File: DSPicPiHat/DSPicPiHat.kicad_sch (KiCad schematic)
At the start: 84 parts

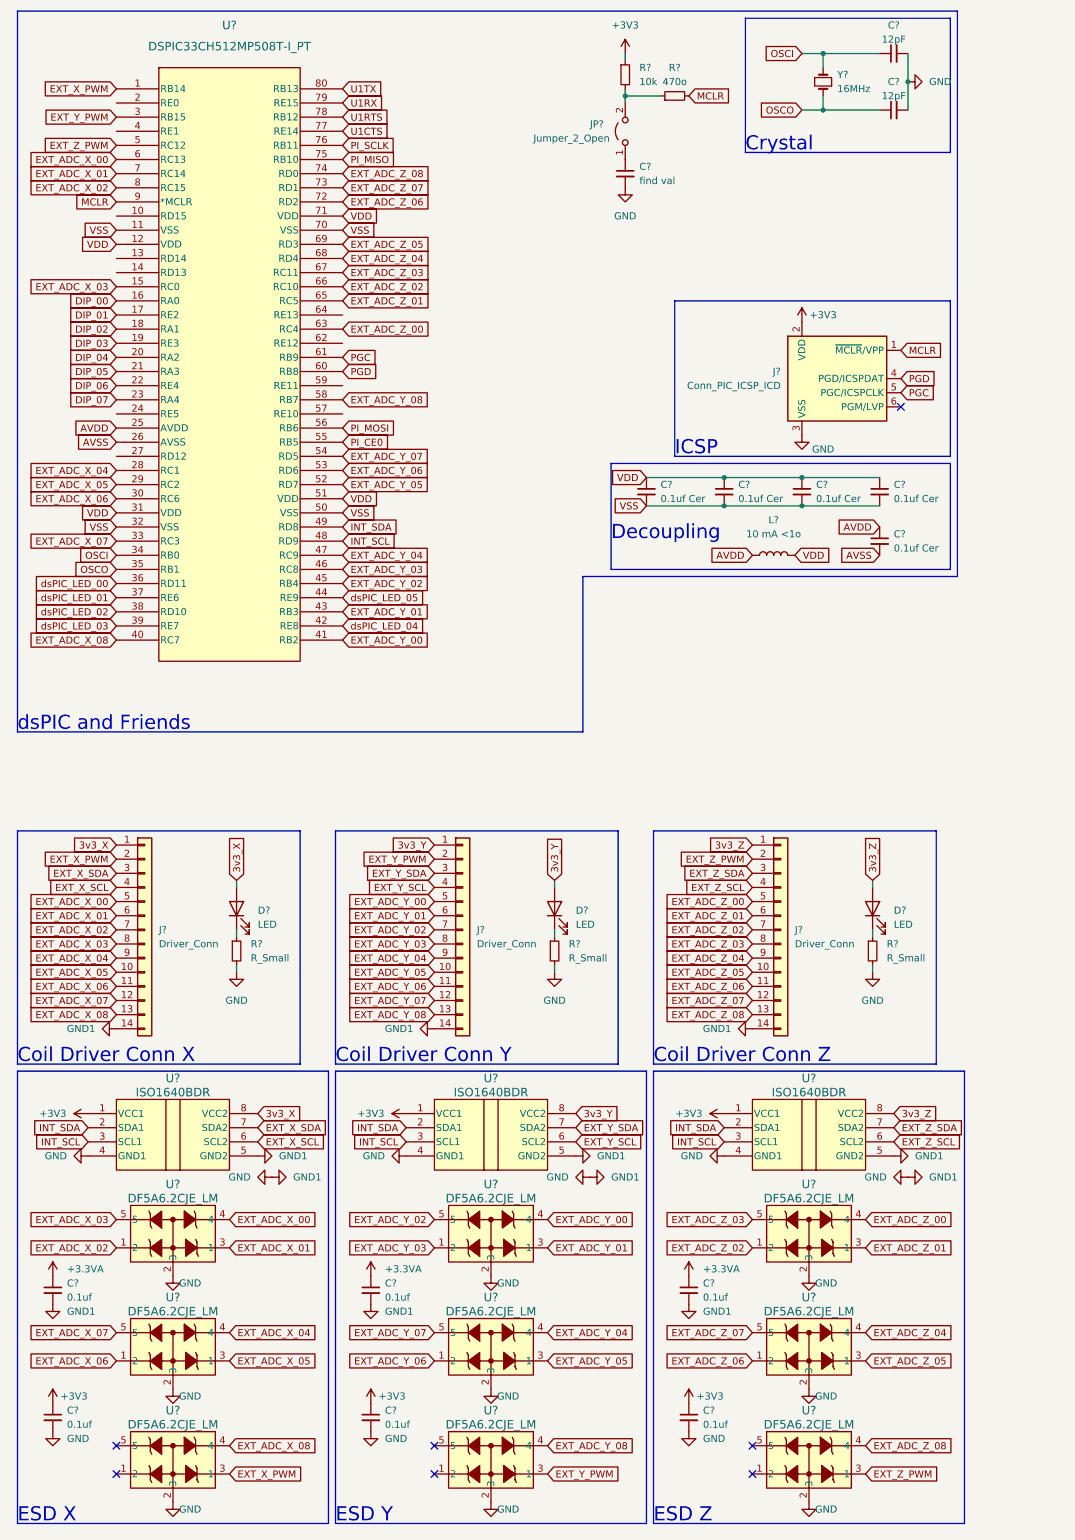
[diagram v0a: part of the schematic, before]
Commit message: fix connector connections and remove extra ones, switches resistor array for multiple resistors
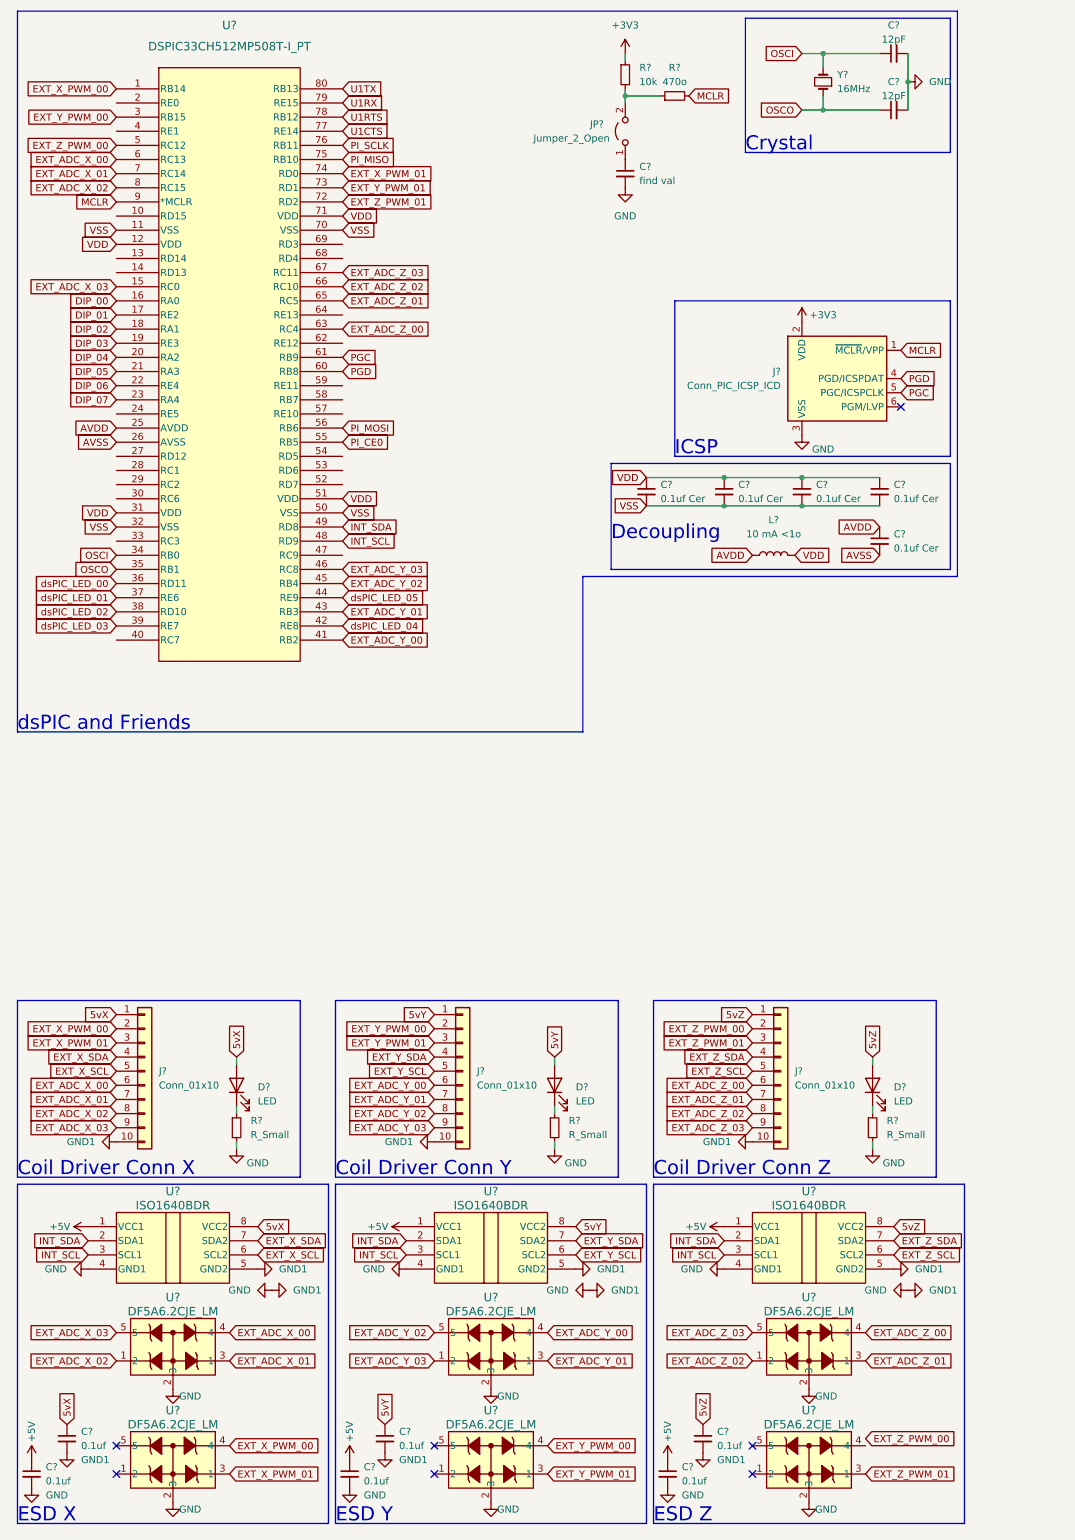
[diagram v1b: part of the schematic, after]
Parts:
- removed J? (x3): Driver_Conn, symbol Connector_Generic:Conn_01x14
- removed U? (x3): DF5A6.2CJE_LM, SOT-553 ESV_TOS, symbol PiHatLib:DF5A6.2CJE_LM
- added J? (x3): Conn_01x10, symbol Connector_Generic:Conn_01x10
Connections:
- net +3V3: no longer C?.1, C?.1, C?.1, U?.1 (VCC1), U?.1 (VCC1), U?.1 (VCC1)
- net +5V: now also C?.1, C?.1, C?.1, U?.1 (VCC1), U?.1 (VCC1), U?.1 (VCC1)
- net EXT_ADC_X_00: now also J?.6 (Pin_6)
- net EXT_ADC_X_01: now also J?.7 (Pin_7)
- net EXT_ADC_X_02: now also J?.8 (Pin_8)
- net EXT_ADC_X_03: now also J?.9 (Pin_9)
- net EXT_ADC_Y_00: now also J?.6 (Pin_6)
- net EXT_ADC_Y_01: now also J?.7 (Pin_7)
- net EXT_ADC_Y_02: now also J?.8 (Pin_8)
- net EXT_ADC_Y_03: now also J?.9 (Pin_9)
- net EXT_ADC_Z_00: now also J?.6 (Pin_6)
- net EXT_ADC_Z_01: now also J?.7 (Pin_7)
- net EXT_ADC_Z_02: now also J?.8 (Pin_8)
- net EXT_ADC_Z_03: now also J?.9 (Pin_9)
- net EXT_X_SCL: now also J?.5 (Pin_5)
- net EXT_X_SDA: now also J?.4 (Pin_4)
- net EXT_Y_SCL: now also J?.5 (Pin_5)
- net EXT_Y_SDA: now also J?.4 (Pin_4)
- net EXT_Z_SCL: now also J?.5 (Pin_5)
- net EXT_Z_SDA: now also J?.4 (Pin_4)
- net GND: now also J?.10 (Pin_10), J?.10 (Pin_10), J?.10 (Pin_10)
- removed net +3.3VA: C?.1, C?.1, C?.1
- net 3v3_X renamed 5vX
- net 5vX: now also C?.1, J?.1 (Pin_1)
- net 3v3_Y renamed 5vY
- net 5vY: now also C?.1, J?.1 (Pin_1)
- net 3v3_Z renamed 5vZ
- net 5vZ: now also C?.1, J?.1 (Pin_1)
- net EXT_ADC_X_04: no longer names the net of U?.28 (RC1)
- net EXT_ADC_X_05: no longer names the net of U?.29 (RC2)
- net EXT_ADC_X_06: no longer names the net of U?.30 (RC6)
- net EXT_ADC_X_07: no longer names the net of U?.33 (RC3)
- net EXT_ADC_X_08: no longer names the net of U?.40 (RC7)
- net EXT_ADC_X_08: no longer U?.4
- net EXT_ADC_Y_04: no longer names the net of U?.47 (RC9)
- net EXT_ADC_Y_05: no longer names the net of U?.52 (RD7)
- net EXT_ADC_Y_06: no longer names the net of U?.53 (RD6)
- net EXT_ADC_Y_07: no longer names the net of U?.54 (RD5)
- net EXT_ADC_Y_08: no longer names the net of U?.58 (RB7)
- net EXT_ADC_Y_08: no longer U?.4
- net EXT_ADC_Z_04: no longer names the net of U?.68 (RD4)
- net EXT_ADC_Z_05: no longer names the net of U?.69 (RD3)
- net EXT_ADC_Z_06 renamed EXT_Z_PWM_01
- net EXT_Z_PWM_01: now also U?.3 (1), J?.3 (Pin_3)
- net EXT_ADC_Z_07 renamed EXT_Y_PWM_01
- net EXT_Y_PWM_01: now also U?.3 (1), J?.3 (Pin_3)
- net EXT_ADC_Z_08: no longer names the net of U?.4
- net EXT_ADC_Z_08: no longer U?.74 (RD0)
- net EXT_X_PWM renamed EXT_X_PWM_00
- net EXT_X_PWM_00: now also U?.4, J?.2 (Pin_2); no longer U?.3 (1)
- net EXT_Y_PWM renamed EXT_Y_PWM_00
- net EXT_Y_PWM_00: now also U?.4, J?.2 (Pin_2); no longer U?.3 (1)
- net EXT_Z_PWM renamed EXT_Z_PWM_00
- net EXT_Z_PWM_00: now also J?.2 (Pin_2); no longer U?.3 (1)
- new net EXT_X_PWM_01: J?.3 (Pin_3), U?.3 (1), U?.74 (RD0)
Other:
- moved on the sheet: C?, D?, R?, U?

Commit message: start adding pcb footprints, working on pcb outline, and starting routing.
Also removed resistor array.
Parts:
- removed RN?: 10k, Resistor_THT:R_Array_SIP9, symbol Device:R_Network08
- added R17, R18, R19, R20, R21, R22, R23, R24: 10k, Resistor_SMD:R_0805_2012Metric, symbol Device:R_Small
- C1, C10, C11, C12, C13, C14, C15, C16, C17, C18, C2, C20, C21, C3, C4, C5, C6, C7, C8, C9: renamed from C?; footprint (none) -> Capacitor_SMD:C_0805_2012Metric
- Connector_X1, Connector_Y1, Connector_Z1: renamed from J?; footprint (none) -> Connector_Molex:Molex_Micro-Fit_3.0_43045-1012_2x05_P3.00mm_Vertical
- D1, D10, D11, D2, D3, D6, D7, D8, D9: renamed from D?; footprint (none) -> LED_SMD:LED_0805_2012Metric
- J10: renamed from J?; footprint (none) -> Connector_PinSocket_2.54mm:PinSocket_1x05_P2.54mm_Vertical
- J4: renamed from J?; footprint (none) -> Connector_PinHeader_2.54mm:PinHeader_2x03_P2.54mm_Vertical
- J5: renamed from J?; footprint (none) -> Connector_USB:USB_C_Receptacle_HRO_TYPE-C-31-M-12
- J6: renamed from J?; footprint (none) -> Connector_Molex:Molex_Micro-Fit_3.0_43045-0212_2x01_P3.00mm_Vertical
- J7, J9: renamed from J?; footprint (none) -> Connector_PinSocket_2.54mm:PinSocket_1x08_P2.54mm_Vertical
- J8: renamed from J?; footprint (none) -> Connector_PinSocket_2.54mm:PinSocket_2x20_P2.54mm_Vertical
- R1, R10, R11, R12, R13, R14, R15, R16, R2, R3, R4, R5, R6, R7, R8, R9: renamed from R?; footprint (none) -> Resistor_SMD:R_0805_2012Metric
- SW1: renamed from SW?; footprint (none) -> Button_Switch_SMD:SW_SPDT_PCM12
- SW2: renamed from SW?; footprint (none) -> Button_Switch_THT:SW_DIP_SPSTx08_Slide_9.78x22.5mm_W7.62mm_P2.54mm
- U1: renamed from U?; footprint TQFP80_12x12MC_MCH -> Package_QFP:TQFP-80_12x12mm_P0.5mm
- U10, U3, U4, U6, U7, U9: renamed from U?; footprint SOT-553 ESV_TOS -> Package_TO_SOT_SMD:SOT-553
- U2, U5, U8: renamed from U?; footprint D0008B-IPC_A -> Package_SO:SOIC-8-1EP_3.9x4.9mm_P1.27mm_EP2.29x3mm
- gave numbers to parts that had none: 13
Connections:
- net +5V: now also R17.1, R18.1, R19.1, R20.1, R21.1, R22.1, R23.1, R24.1
- net 5vX: now also Connector_X1.10 (Pin_10); no longer Connector_X1.1 (Pin_1)
- net 5vY: now also Connector_Y1.10 (Pin_10); no longer Connector_Y1.1 (Pin_1)
- net 5vZ: now also Connector_Z1.10 (Pin_10); no longer Connector_Z1.1 (Pin_1)
- net DIP_00: now also R17.2
- net DIP_01: now also R18.2
- net DIP_02: now also R19.2
- net DIP_03: now also R20.2
- net DIP_04: now also R21.2
- net DIP_05: now also R22.2
- net DIP_06: now also R23.2
- net DIP_07: now also R24.2
- net EXT_ADC_X_00: now also U4.4; no longer U3.4
- net EXT_ADC_X_01: now also U4.5; no longer U3.3 (1)
- net EXT_ADC_X_02: now also U3.3 (1); no longer U3.1 (2)
- net EXT_ADC_X_03: now also U3.4; no longer U3.5
- net EXT_X_PWM_00: now also U3.5; no longer U4.4
- net EXT_X_PWM_01: now also U3.1 (2); no longer U4.3 (1)
- net GND: now also Connector_X1.1 (Pin_1), Connector_Z1.1 (Pin_1); no longer C2.2, C4.2, C8.2, Connector_X1.10 (Pin_10), Connector_Y1.10 (Pin_10), Connector_Z1.10 (Pin_10), U5.5 (GND2)
- new net GND1: C2.2, C4.2, C8.2
- new net GNDY: Connector_Y1.1 (Pin_1), U5.5 (GND2)
- no-connect marks 8 -> 10
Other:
- moved on the sheet: C1, C2

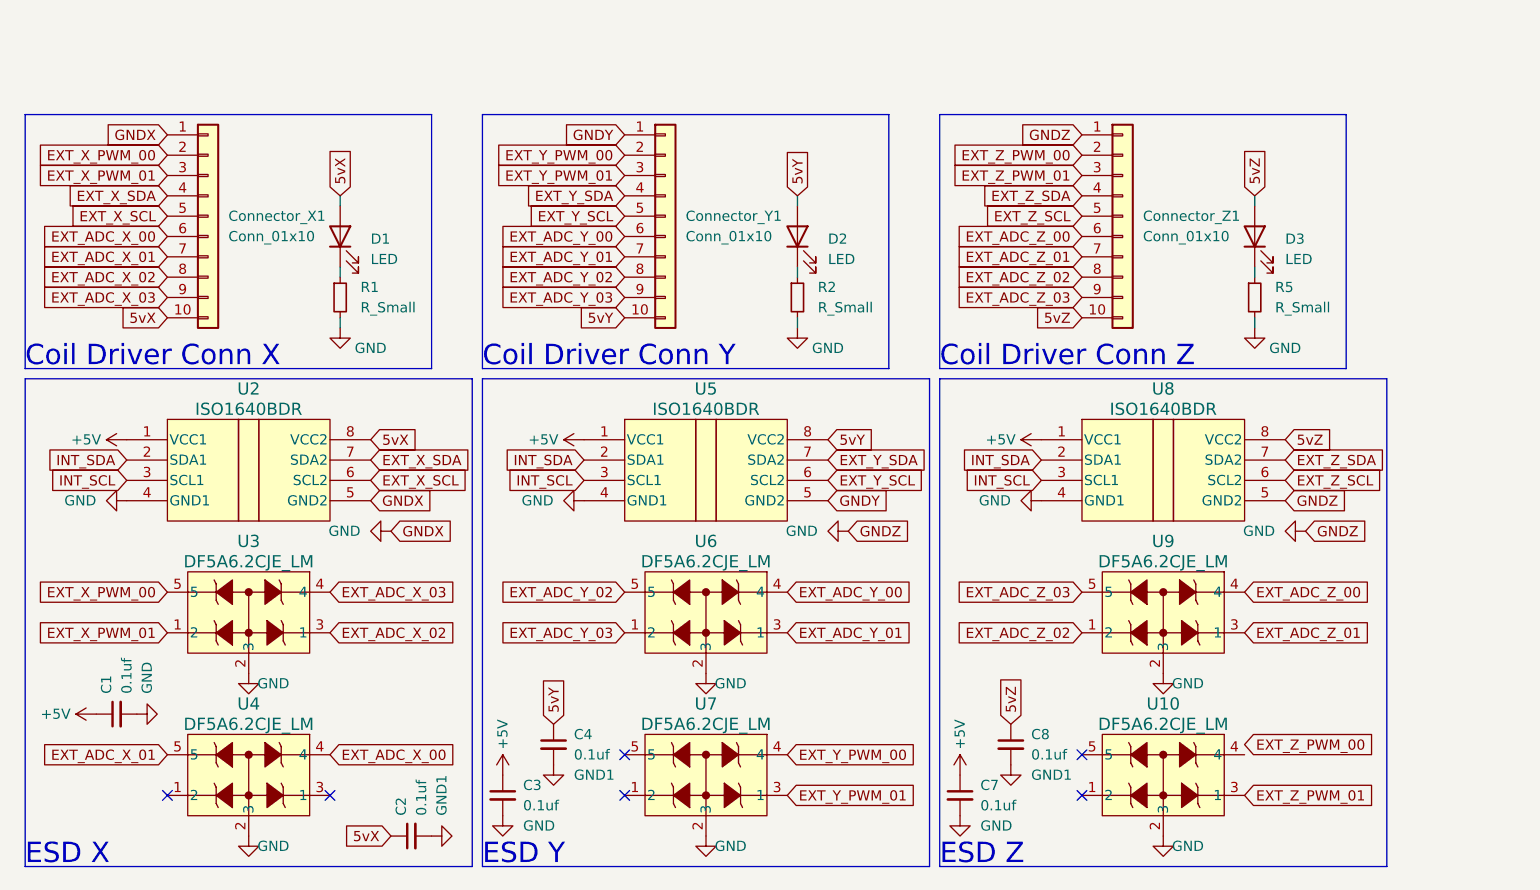
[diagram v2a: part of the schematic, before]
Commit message: ESD connected to axis connectors.
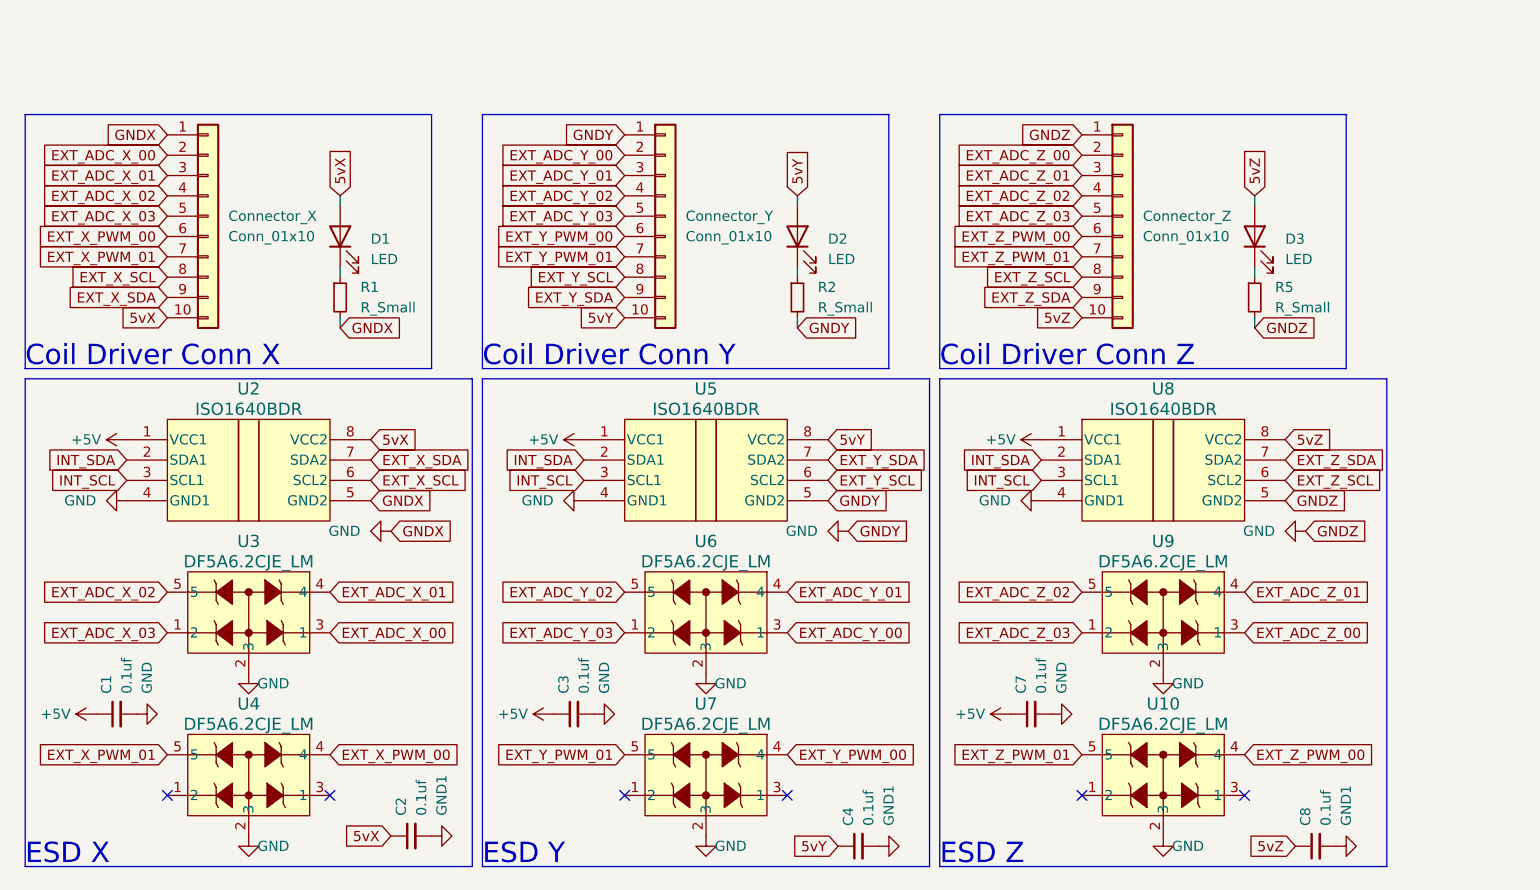
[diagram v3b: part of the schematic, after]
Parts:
- renumbered Connector_X1 to Connector_X, Connector_Y1 to Connector_Y, Connector_Z1 to Connector_Z
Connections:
- net GNDY is gone; now on net GND: Connector_Y.1 (Pin_1), U5.5 (GND2)
- net EXT_ADC_X_00: now also Connector_X.2 (Pin_2), U3.3 (1); no longer Connector_X.6 (Pin_6), U4.4
- net EXT_ADC_X_01: now also Connector_X.3 (Pin_3), U3.4; no longer Connector_X.7 (Pin_7), U4.5
- net EXT_ADC_X_02: now also Connector_X.4 (Pin_4), U3.5; no longer Connector_X.8 (Pin_8), U3.3 (1)
- net EXT_ADC_X_03: now also Connector_X.5 (Pin_5), U3.1 (2); no longer Connector_X.9 (Pin_9), U3.4
- net EXT_ADC_Y_00: now also Connector_Y.2 (Pin_2), U6.3 (1); no longer Connector_Y.6 (Pin_6), U6.4
- net EXT_ADC_Y_01: now also Connector_Y.3 (Pin_3), U6.4; no longer Connector_Y.7 (Pin_7), U6.3 (1)
- net EXT_ADC_Y_02: now also Connector_Y.4 (Pin_4); no longer Connector_Y.8 (Pin_8)
- net EXT_ADC_Y_03: now also Connector_Y.5 (Pin_5); no longer Connector_Y.9 (Pin_9)
- net EXT_ADC_Z_00: now also Connector_Z.2 (Pin_2), U9.3 (1); no longer Connector_Z.6 (Pin_6), U9.4
- net EXT_ADC_Z_01: now also Connector_Z.3 (Pin_3), U9.4; no longer Connector_Z.7 (Pin_7), U9.3 (1)
- net EXT_ADC_Z_02: now also Connector_Z.4 (Pin_4), U9.5; no longer Connector_Z.8 (Pin_8), U9.1 (2)
- net EXT_ADC_Z_03: now also Connector_Z.5 (Pin_5), U9.1 (2); no longer Connector_Z.9 (Pin_9), U9.5
- net EXT_X_PWM_00: now also Connector_X.6 (Pin_6), U4.4; no longer Connector_X.2 (Pin_2), U3.5
- net EXT_X_PWM_01: now also Connector_X.7 (Pin_7), U4.5; no longer Connector_X.3 (Pin_3), U3.1 (2)
- net EXT_X_SCL: now also Connector_X.8 (Pin_8); no longer Connector_X.5 (Pin_5)
- net EXT_X_SDA: now also Connector_X.9 (Pin_9); no longer Connector_X.4 (Pin_4)
- net EXT_Y_PWM_00: now also Connector_Y.6 (Pin_6); no longer Connector_Y.2 (Pin_2)
- net EXT_Y_PWM_01: now also Connector_Y.7 (Pin_7), U7.5; no longer Connector_Y.3 (Pin_3), U7.3 (1)
- net EXT_Y_SCL: now also Connector_Y.8 (Pin_8); no longer Connector_Y.5 (Pin_5)
- net EXT_Y_SDA: now also Connector_Y.9 (Pin_9); no longer Connector_Y.4 (Pin_4)
- net EXT_Z_PWM_00: now also Connector_Z.6 (Pin_6), U10.4; no longer Connector_Z.2 (Pin_2)
- net EXT_Z_PWM_01: now also Connector_Z.7 (Pin_7), U10.5; no longer Connector_Z.3 (Pin_3), U10.3 (1)
- net EXT_Z_SCL: now also Connector_Z.8 (Pin_8); no longer Connector_Z.5 (Pin_5)
- net EXT_Z_SDA: now also Connector_Z.9 (Pin_9); no longer Connector_Z.4 (Pin_4)
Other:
- moved on the sheet: C3, C4, C7, C8
